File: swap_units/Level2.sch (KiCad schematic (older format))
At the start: 3 parts, among them U1 LM324

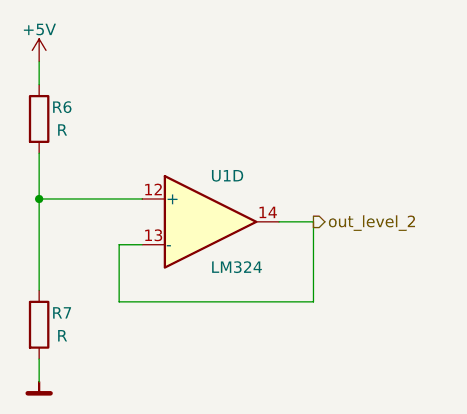
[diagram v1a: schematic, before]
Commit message: Updated test project to include multiple hierarchy
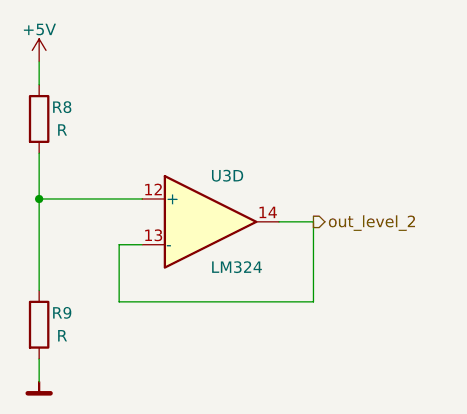
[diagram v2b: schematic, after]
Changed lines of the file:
@@
 $Descr A4 11693 8268
 encoding utf-8
-Sheet 3 3
+Sheet 4 4
 Title ""
 Date ""
@@
 U 4 1 5B2A1811
 P 3900 3800
-F 0 "U1" H 3900 4000 50  0000 L CNN
+AR Path="/5B2A1286/5B2A1299/5B2A1811" Ref="U1"  Part="4"
+AR Path="/5B2A1286/5C9CDC4B/5B2A1811" Ref="U3"  Part="4"
+F 0 "U3" H 3900 4000 50  0000 L CNN
 F 1 "LM324" H 3900 3600 50  0000 L CNN
 F 2 "Package_DIP:DIP-14_W7.62mm" H 3850 3900 50  0001 C CNN
@@
 U 1 1 5B2A4F5C
 P 3150 3350
-F 0 "R6" H 3250 3400 50  0000 C CNN
+AR Path="/5B2A1286/5B2A1299/5B2A4F5C" Ref="R6"  Part="1"
+AR Path="/5B2A1286/5C9CDC4B/5B2A4F5C" Ref="R8"  Part="1"
+F 0 "R8" H 3250 3400 50  0000 C CNN
 F 1 "R" H 3250 3300 50  0000 C CNN
 F 2 "Resistor_THT:R_Axial_DIN0207_L6.3mm_D2.5mm_P10.16mm_Horizontal" V 3080 3350 50  0001 C CNN
@@
 U 1 1 5B2A4F63
 P 3150 4250
-F 0 "R7" H 3250 4300 50  0000 C CNN
+AR Path="/5B2A1286/5B2A1299/5B2A4F63" Ref="R7"  Part="1"
+AR Path="/5B2A1286/5C9CDC4B/5B2A4F63" Ref="R9"  Part="1"
+F 0 "R9" H 3250 4300 50  0000 C CNN
 F 1 "R" H 3250 4200 50  0000 C CNN
 F 2 "Resistor_THT:R_Axial_DIN0207_L6.3mm_D2.5mm_P10.16mm_Horizontal" V 3080 4250 50  0001 C CNN
@@
 U 1 1 5B2A4F6A
 P 3150 3100
-F 0 "#PWR09" H 3150 2950 50  0001 C CNN
+AR Path="/5B2A1286/5B2A1299/5B2A4F6A" Ref="#PWR09"  Part="1"
+AR Path="/5B2A1286/5C9CDC4B/5B2A4F6A" Ref="#PWR011"  Part="1"
+F 0 "#PWR011" H 3150 2950 50  0001 C CNN
 F 1 "+5V" H 3150 3240 50  0000 C CNN
 F 2 "" H 3150 3100 50  0001 C CNN
@@
 U 1 1 5B2A4F70
 P 3150 4500
-F 0 "#PWR010" H 3150 4350 50  0001 C CNN
+AR Path="/5B2A1286/5B2A1299/5B2A4F70" Ref="#PWR010"  Part="1"
+AR Path="/5B2A1286/5C9CDC4B/5B2A4F70" Ref="#PWR012"  Part="1"
+F 0 "#PWR012" H 3150 4350 50  0001 C CNN
 F 1 "GND" H 3300 4450 50  0001 C CNN
 F 2 "" H 3150 4500 50  0001 C CNN
